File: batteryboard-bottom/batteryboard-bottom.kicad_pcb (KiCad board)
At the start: 2 copper layers, 46.8 x 46.8 mm, 7 parts, among them J1 SFC-110-T2-F-D-A, J2 FTS-107-01-L-DV-A

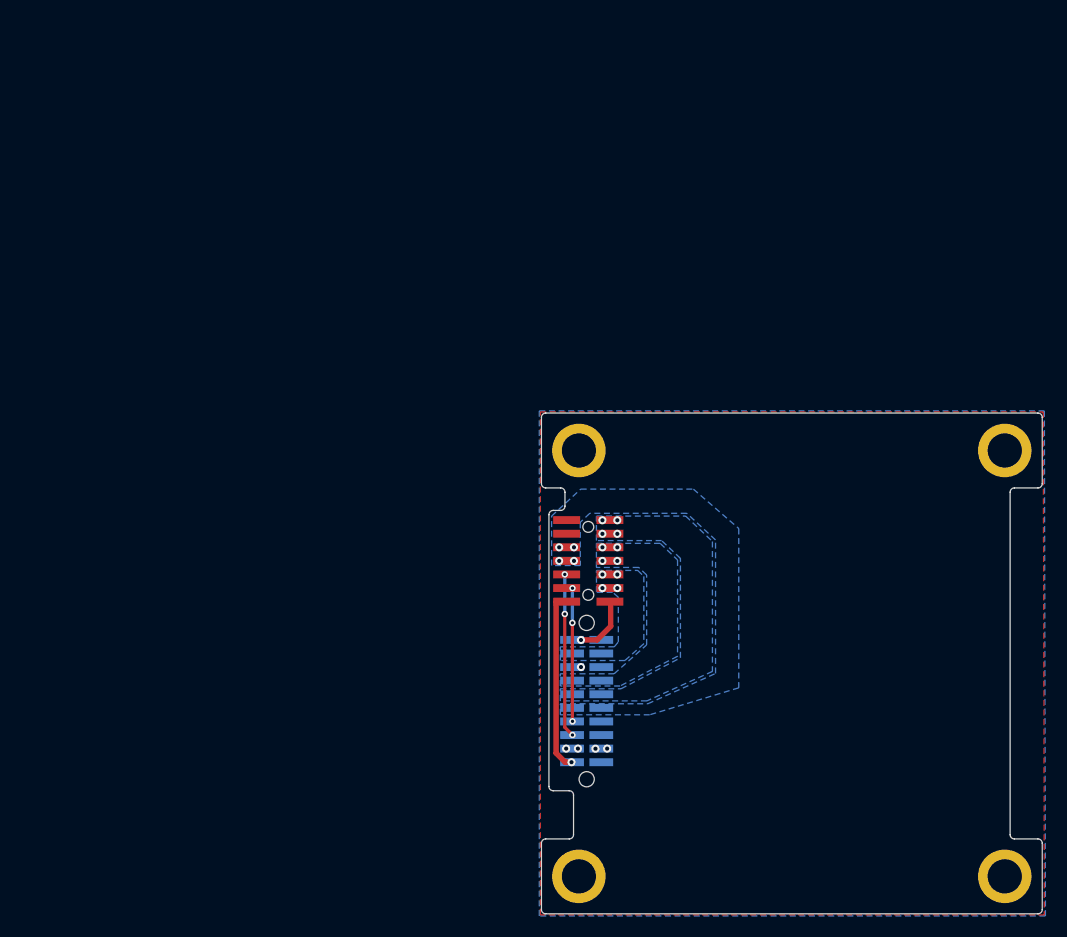
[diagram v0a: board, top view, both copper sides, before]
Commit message: Updated batteryboards for Rev B3/01
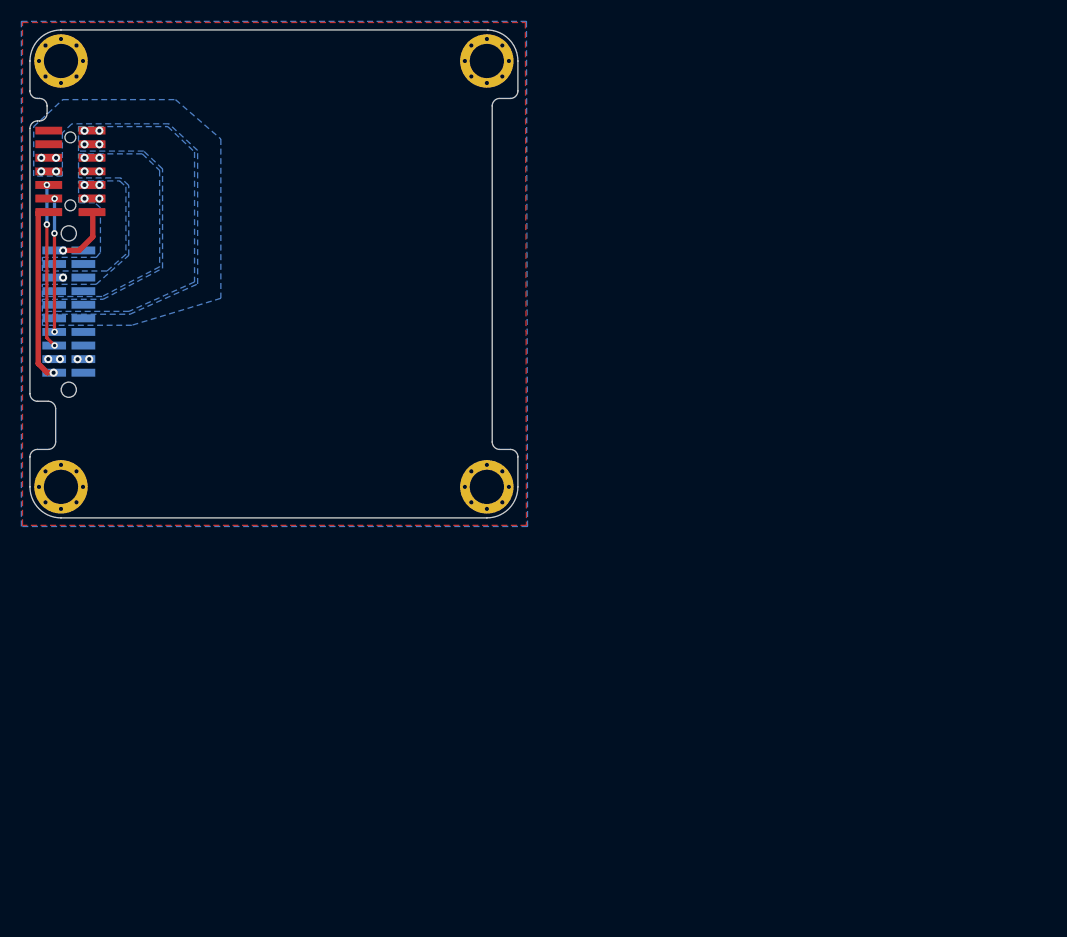
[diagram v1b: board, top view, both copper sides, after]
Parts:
- J1: value SFC-110-T2-F-D-A -> SFC-110-T2-X-D-A; footprint mainboard:SAMTEC_SFC-110-T2-F-D-A-TR -> mainboard:SAMTEC_SFC-110-T2-X-D-A
- J2: value FTS-107-01-L-DV-A -> FTS-107-01-X-DV-A
- moved Ref** 60.7 mm to (104.5, 44.9)
- moved H4 60.6 mm to (84.4, 45.4)
- moved J1 60.6 mm to (85.1, 68.8)
- moved J2 60.6 mm to (85.3, 55.7)
- moved H3 60.6 mm to (84.4, 85.2)
- moved H1 60.6 mm to (124.2, 45.4)
- moved H2 60.6 mm to (124.2, 85.2)
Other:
- board size 46.8 x 46.8 mm -> 45.6 x 45.6 mm
- board text added: "18-FEB-23"
- board text added: "Rev B3/01"
- board text removed: "06-NOV-22"
- board text removed: "Rev B2/01"

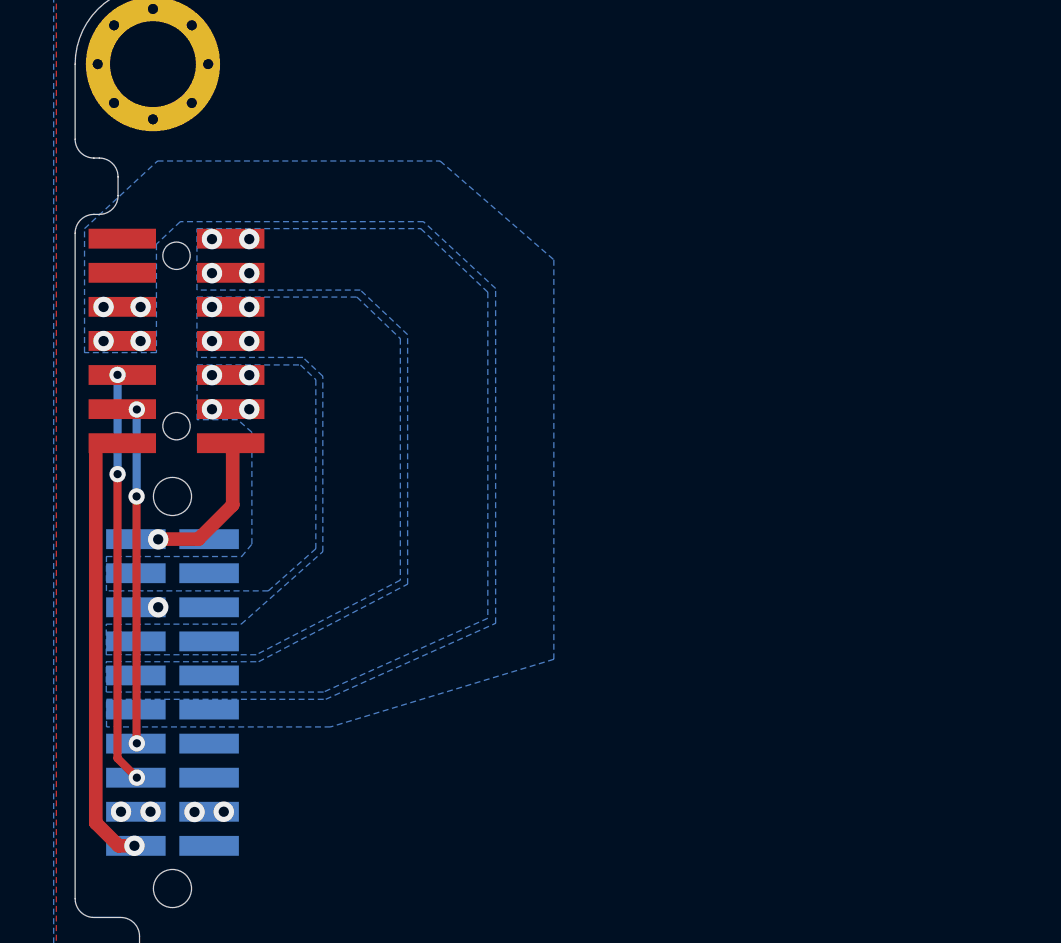
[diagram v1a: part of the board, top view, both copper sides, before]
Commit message: Added battery current sensing to bottom batteryboard
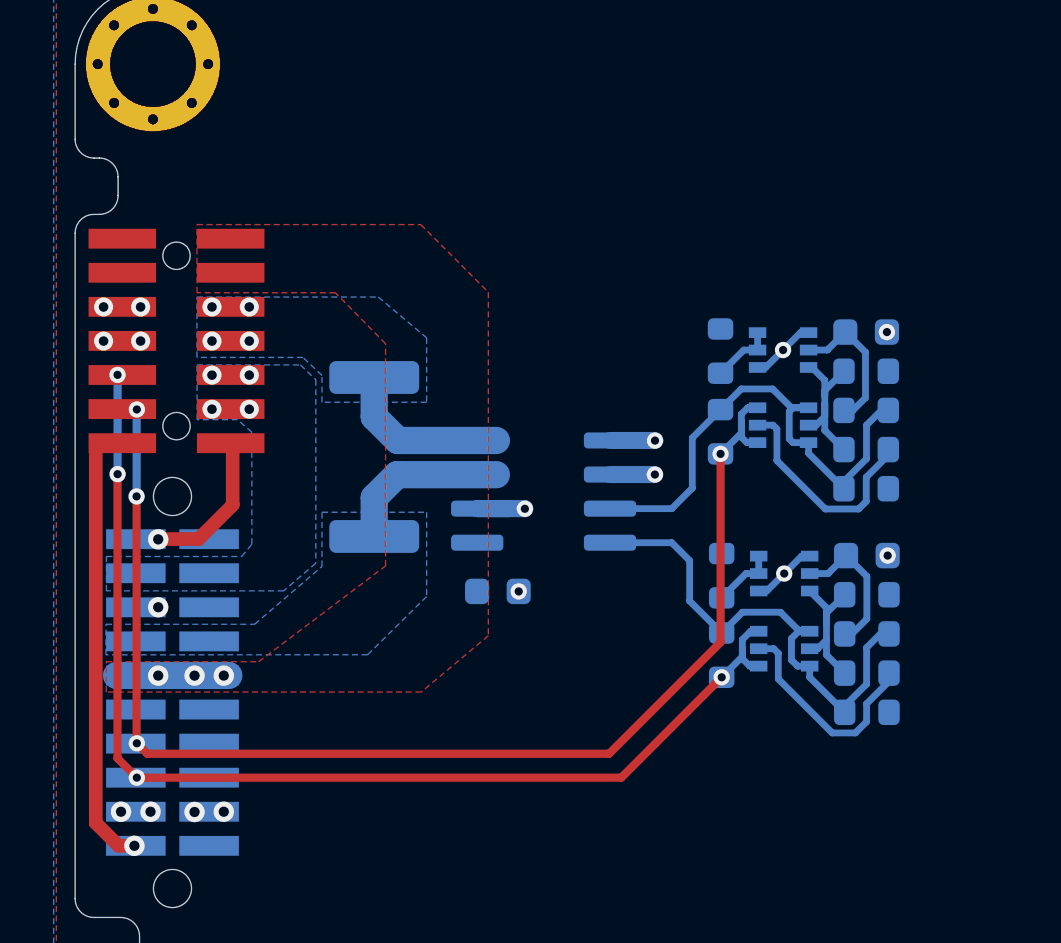
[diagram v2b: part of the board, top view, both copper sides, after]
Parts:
- added C1: 10nF, Capacitor_SMD:C_0603_1608Metric, B.Cu at (111.0, 63.7)
- added C2: 10nF, Capacitor_SMD:C_0603_1608Metric, B.Cu at (111.0, 55.4)
- added C3: 0.1uF, Capacitor_SMD:C_0603_1608Metric, B.Cu at (97.3, 65.0)
- added Q1: NX3008NBKS, Package_TO_SOT_SMD:SOT-363_SC-70-6, B.Cu at (107.9, 64.4)
- added Q2: MBT2222ADW1T1, Package_TO_SOT_SMD:SOT-363_SC-70-6, B.Cu at (107.9, 67.2)
- added Q3: NX3008NBKS, Package_TO_SOT_SMD:SOT-363_SC-70-6, B.Cu at (107.9, 56.1)
- added Q4: MBT2222ADW1T1, Package_TO_SOT_SMD:SOT-363_SC-70-6, B.Cu at (107.9, 58.9)
- added R1: 0.04R, Resistor_SMD:R_2512_6332Metric, B.Cu at (92.6, 60.0)
- added R10: 10K, Resistor_SMD:R_0603_1608Metric, B.Cu at (111.0, 61.2)
- added R11: 200K, Resistor_SMD:R_0603_1608Metric, B.Cu at (111.0, 58.3)
- added R12: DNI (0R), Resistor_SMD:R_0603_1608Metric, B.Cu at (105.6, 67.4)
- added R13: DNI (0R), Resistor_SMD:R_0603_1608Metric, B.Cu at (105.6, 59.1)
- added R2: 680R, Resistor_SMD:R_0603_1608Metric, B.Cu at (111.0, 68.1)
- added R3: 100K, Resistor_SMD:R_0603_1608Metric, B.Cu at (105.6, 64.5)
- added R4: 10K, Resistor_SMD:R_0603_1608Metric, B.Cu at (111.0, 65.2)
- added R5: 10K, Resistor_SMD:R_0603_1608Metric, B.Cu at (111.0, 69.6)
- added R6: 200K, Resistor_SMD:R_0603_1608Metric, B.Cu at (111.0, 66.6)
- added R7: 680R, Resistor_SMD:R_0603_1608Metric, B.Cu at (111.0, 59.8)
- added R8: 100K, Resistor_SMD:R_0603_1608Metric, B.Cu at (105.6, 56.1)
- added R9: 10K, Resistor_SMD:R_0603_1608Metric, B.Cu at (111.0, 56.8)
- added U1: INA219BxD, Package_SO:SOIC-8_3.9x4.9mm_P1.27mm, B.Cu at (99.0, 61.3)
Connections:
- J2 pad 6: BATT_P_SW -> BATT_P_SENSE
- J2 pad 8: BATT_P_SW -> BATT_P_SENSE
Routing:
- net SDA1: track 12.4 -> 46.9 mm, vias 3 -> 4
- net SCL1: track 15.3 -> 42.2 mm, vias 3 -> 4
- net SDA_C_SENSE: track 0.00 -> 18.7 mm
- net SCL_C_SENSE: track 0.00 -> 18.6 mm
- net GND: track 0.00 -> 11.2 mm, vias 5 -> 13
- net Net-(Q4A-B1): track 0.00 -> 8.21 mm
- net Net-(Q2A-B1): track 0.00 -> 7.91 mm
- net BATT_P_SENSE: track 0.00 -> 6.39 mm, vias 0 -> 4
- net BATT_P_SW: track 0.00 -> 6.36 mm, vias 4 -> 0
- net Net-(Q3A-D1): track 0.00 -> 5.98 mm
- net Net-(Q1A-D1): track 0.00 -> 5.71 mm
- net Net-(Q3B-G1): track 0.00 -> 5.40 mm
- net Net-(Q1B-G1): track 0.00 -> 5.11 mm
- net BATT_N_SW: track 0.00 -> 4.19 mm, vias 4 -> 3
- net Net-(Q1A-G2): track 0.00 -> 2.40 mm
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- added copper zone on F.Cu, net BATT_N_SW
- added copper zone on B.Cu, net BATT_P_SENSE
- removed copper zone on B.Cu, net BATT_N_SW
- removed copper zone on B.Cu, net GND
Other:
- rule pad_to_mask_clearance: 0 -> 0.0508

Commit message: Exported Gerbers
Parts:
- renumbered H4 to Hw
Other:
- rule pad_to_mask_clearance: 0.0508 -> 0

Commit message: Rev B3/02 updates
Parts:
- added REF**: Fiducial_1mm_Mask2mm, Fiducial:Fiducial_1mm_Mask2mm, F.Cu at (120.2, 85.2)
- added REF**: Fiducial_1mm_Mask2mm, Fiducial:Fiducial_1mm_Mask2mm, F.Cu at (120.2, 45.4)
- added REF**: Fiducial_1mm_Mask2mm, Fiducial:Fiducial_1mm_Mask2mm, F.Cu at (88.4, 45.4)
- added REF**: Fiducial_1mm_Mask2mm, Fiducial:Fiducial_1mm_Mask2mm, B.Cu at (120.2, 85.2)
- added REF**: Fiducial_1mm_Mask2mm, Fiducial:Fiducial_1mm_Mask2mm, B.Cu at (120.2, 45.4)
- added REF**: Fiducial_1mm_Mask2mm, Fiducial:Fiducial_1mm_Mask2mm, B.Cu at (88.4, 45.4)
- R1: footprint Resistor_SMD:R_2512_6332Metric -> batteryboard:R_2512_CurrentSense
- moved Ref** 0.51 mm to (105.0, 44.8)
- renumbered Hw to H4
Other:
- outline, holes or cut-outs redrawn
- board text added: "12-APR-23"
- board text added: "Rev B3/02"
- board text removed: "18-FEB-23"
- board text removed: "Rev B3/01"

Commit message: Rev B3/03 updates
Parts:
- added C4: 0.1uF, Capacitor_SMD:C_0603_1608Metric, B.Cu at (112.5, 56.4)
- added C5: 0.1uF, Capacitor_SMD:C_0603_1608Metric, B.Cu at (117.5, 60.6)
- added C6: 22pF, Capacitor_SMD:C_0603_1608Metric, B.Cu at (109.7, 58.8)
- added C7: 22pF, Capacitor_SMD:C_0603_1608Metric, B.Cu at (109.7, 61.9)
- added C8: 10nF, Capacitor_SMD:C_0603_1608Metric, B.Cu at (114.4, 67.4)
- added C9: 10nF, Capacitor_SMD:C_0603_1608Metric, B.Cu at (106.2, 67.4)
- added Q5: NX3008NBKS, Package_TO_SOT_SMD:SOT-363_SC-70-6, B.Cu at (115.1, 70.5)
- added Q6: MBT2222ADW1T1, Package_TO_SOT_SMD:SOT-363_SC-70-6, B.Cu at (117.9, 70.5)
- added Q7: NX3008NBKS, Package_TO_SOT_SMD:SOT-363_SC-70-6, B.Cu at (106.9, 70.5)
- added Q8: MBT2222ADW1T1, Package_TO_SOT_SMD:SOT-363_SC-70-6, B.Cu at (109.7, 70.5)
- added R14: 680R, Resistor_SMD:R_0603_1608Metric, B.Cu at (118.8, 67.4)
- added R15: 100K, Resistor_SMD:R_0603_1608Metric, B.Cu at (115.1, 72.8)
- added R16: 10K, Resistor_SMD:R_0603_1608Metric, B.Cu at (114.0, 56.4)
- added R17: 10K, Resistor_SMD:R_0603_1608Metric, B.Cu at (117.5, 62.0)
- added R18: 10K, Resistor_SMD:R_0603_1608Metric, B.Cu at (115.8, 67.4)
- added R19: 10K, Resistor_SMD:R_0603_1608Metric, B.Cu at (120.2, 67.4)
- added R20: 200K, Resistor_SMD:R_0603_1608Metric, B.Cu at (117.3, 67.4)
- added R21: 680R, Resistor_SMD:R_0603_1608Metric, B.Cu at (110.6, 67.4)
- added R22: 100K, Resistor_SMD:R_0603_1608Metric, B.Cu at (106.9, 72.8)
- added R23: 10K, Resistor_SMD:R_0603_1608Metric, B.Cu at (107.7, 67.4)
- added R24: 10K, Resistor_SMD:R_0603_1608Metric, B.Cu at (112.0, 67.4)
- added R25: 200K, Resistor_SMD:R_0603_1608Metric, B.Cu at (109.1, 67.4)
- added R26: DNI (0R), Resistor_SMD:R_0603_1608Metric, B.Cu at (118.1, 72.8)
- added R27: DNI (0R), Resistor_SMD:R_0603_1608Metric, B.Cu at (109.9, 72.8)
- added U2: BNO085, mainboard:LGA-28, B.Cu at (113.2, 61.3)
- added Y1: 32.768kHz/12.5pF, Crystal:Crystal_SMD_MicroCrystal_CC7V-T1A-2Pin_3.2x1.5mm, B.Cu at (107.8, 60.3)
- moved R5 20.6 mm to (110.1, 49.0), turned to -90 degrees
- moved R2 19.2 mm to (108.7, 49.0), turned to -90 degrees
- moved R6 18.0 mm to (107.2, 49.0), turned to -90 degrees
- moved R4 17.0 mm to (105.8, 49.0), turned to -90 degrees
- moved C2 16.3 mm to (96.0, 49.0), turned to 90 degrees
- moved C1 16.2 mm to (104.3, 49.0), turned to 90 degrees
- moved R9 15.6 mm to (97.5, 49.0), turned to -90 degrees
- moved R10 15.3 mm to (101.8, 49.0), turned to -90 degrees
- moved R11 15.2 mm to (98.9, 49.0), turned to -90 degrees
- moved Q2 15.1 mm to (107.8, 52.1), turned to 90 degrees
- moved R7 15.1 mm to (100.4, 49.0), turned to -90 degrees
- moved R12 13.2 mm to (108.0, 54.4), turned to 0 degrees
- moved Q1 12.6 mm to (105.0, 52.1), turned to 90 degrees
- moved Q3 11.9 mm to (96.7, 52.1), turned to 90 degrees
- moved Q4 10.8 mm to (99.5, 52.1), turned to 90 degrees
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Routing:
- net SCL1: track 42.2 -> 84.1 mm, vias 4 -> 5
- net SDA1: track 46.9 -> 68.3 mm, vias 4 -> 5
- net SCL_IMU: track 0.00 -> 19.1 mm
- net SDA_IMU: track 0.00 -> 17.2 mm
- net SDA_C_SENSE: track 18.7 -> 27.0 mm
- net Net-(Q8A-B1): track 0.00 -> 8.19 mm
- net Net-(Q6A-B1): track 0.00 -> 8.18 mm
- net SCL_C_SENSE: track 18.6 -> 25.5 mm
- net Net-(Q5A-D1): track 0.00 -> 5.95 mm
- net Net-(Q7A-D1): track 0.00 -> 5.81 mm
- net Net-(Q5B-G1): track 0.00 -> 5.38 mm
- net Net-(Q7B-G1): track 0.00 -> 5.38 mm
- net GND: track 11.2 -> 16.1 mm, vias 13 -> 23
- net Net-(U2-XIN32): track 0.00 -> 4.16 mm
- net Net-(U2-CLKSEL1/XOUT32): track 0.00 -> 4.16 mm
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- added copper zone on B.Cu, net GND
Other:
- board text added: "30-JAN-23"
- board text added: "Rev B3/03"
- board text removed: "12-APR-23"
- board text removed: "Rev B3/02"
